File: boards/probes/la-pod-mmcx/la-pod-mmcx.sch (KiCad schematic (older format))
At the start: 13 parts, among them J1 MMCX-J-P-H-ST-EM1, J2 MMCX-J-P-H-ST-EM1, J3 MMCX-J-P-H-ST-EM1, J4 MMCX-J-P-H-ST-EM1, J5 LSHM-120-02.5-L-DV-A-N-K-TR, J6 MMCX-J-P-H-ST-EM1, J7 MMCX-J-P-H-ST-EM1, J8 MMCX-J-P-H-ST-EM1, J9 MMCX-J-P-H-ST-EM1, U1 24Cxx-DFN8

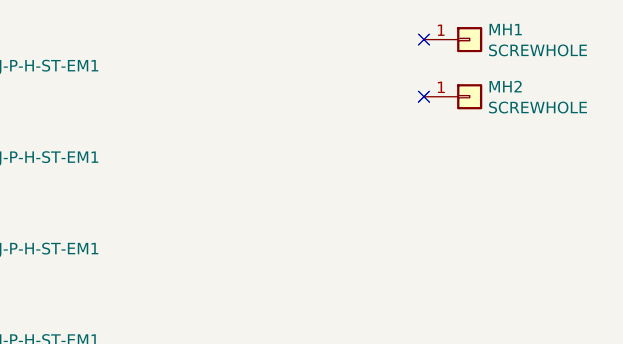
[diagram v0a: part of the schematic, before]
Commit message: Final version of la-pod-mmcx after layout review
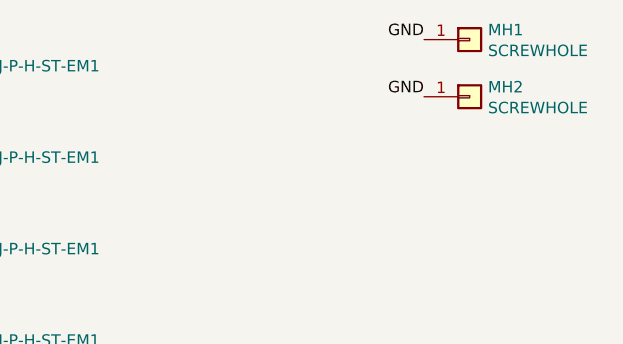
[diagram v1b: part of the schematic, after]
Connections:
- net GND: now also MH1.1 (Pin_1), MH2.1 (Pin_1)
- no-connect marks 2 -> 0
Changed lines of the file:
@@
 Sheet 1 1
 Title "MEAD MMCX input adapter"
-Date "2020-06-02"
+Date "2020-06-03"
 Rev "0.1"
 Comp "Antikernel Labs"
@@
 Text Label 2700 2800 0    50   ~ 0
 I2C_SDA
-NoConn ~ 4850 950
+$Comp
+L Connector:Conn_01x01 MH2
+U 1 1 5ED793A2
+P 5050 1200
+F 0 "MH2" H 5130 1242 50  0000 L CNN
+F 1 "SCREWHOLE" H 5130 1151 50  0000 L CNN
+F 2 "azonenberg_pcb:MECHANICAL_CLEARANCEHOLE_4_40" H 5050 1200 50  0001 C CNN
+F 3 "~" H 5050 1200 50  0001 C CNN
+	1    5050 1200
+	1    0    0    -1
+$EndComp
 $Comp
 L Connector:Conn_01x01 MH1
@@
 	1    0    0    -1
 $EndComp
-$Comp
-L Connector:Conn_01x01 MH2
-U 1 1 5ED793A2
-P 5050 1200
-F 0 "MH2" H 5130 1242 50  0000 L CNN
-F 1 "SCREWHOLE" H 5130 1151 50  0000 L CNN
-F 2 "azonenberg_pcb:MECHANICAL_CLEARANCEHOLE_4_40" H 5050 1200 50  0001 C CNN
-F 3 "~" H 5050 1200 50  0001 C CNN
-	1    5050 1200
-	1    0    0    -1
-$EndComp
-NoConn ~ 4850 1200
+Text Label 4850 950  2    50   ~ 0
+GND
+Text Label 4850 1200 2    50   ~ 0
+GND
 $EndSCHEMATC
